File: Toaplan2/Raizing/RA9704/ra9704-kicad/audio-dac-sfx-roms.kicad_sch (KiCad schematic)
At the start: 6 parts, among them U823 YM2151, U827 27C040, U828 M6295, U829 27C040, U830 M6295

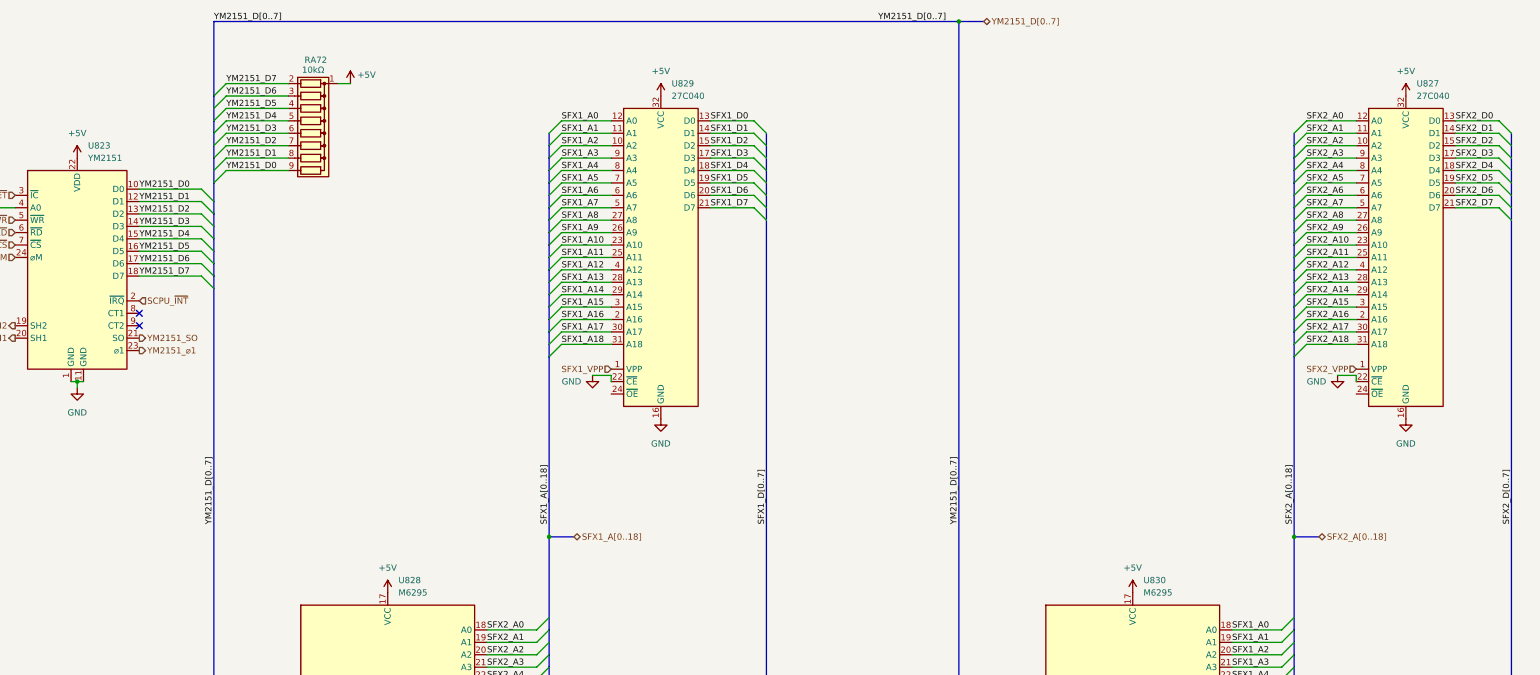
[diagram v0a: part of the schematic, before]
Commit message: fix(ra9704): Add Os as a proxy for 0s in all reference designators
RA9704 has reference designators such that each number has a preceding zero (e.g. RA076, U074, etc.). This causes a bug in KiCAD.

This is 'fixed' by using the 'O' (the letter 'Oh') character instead.

For more info, see the following issue on the KiCAD Gitlab repo

https://gitlab.com/kicad/code/kicad/-/issues/19229
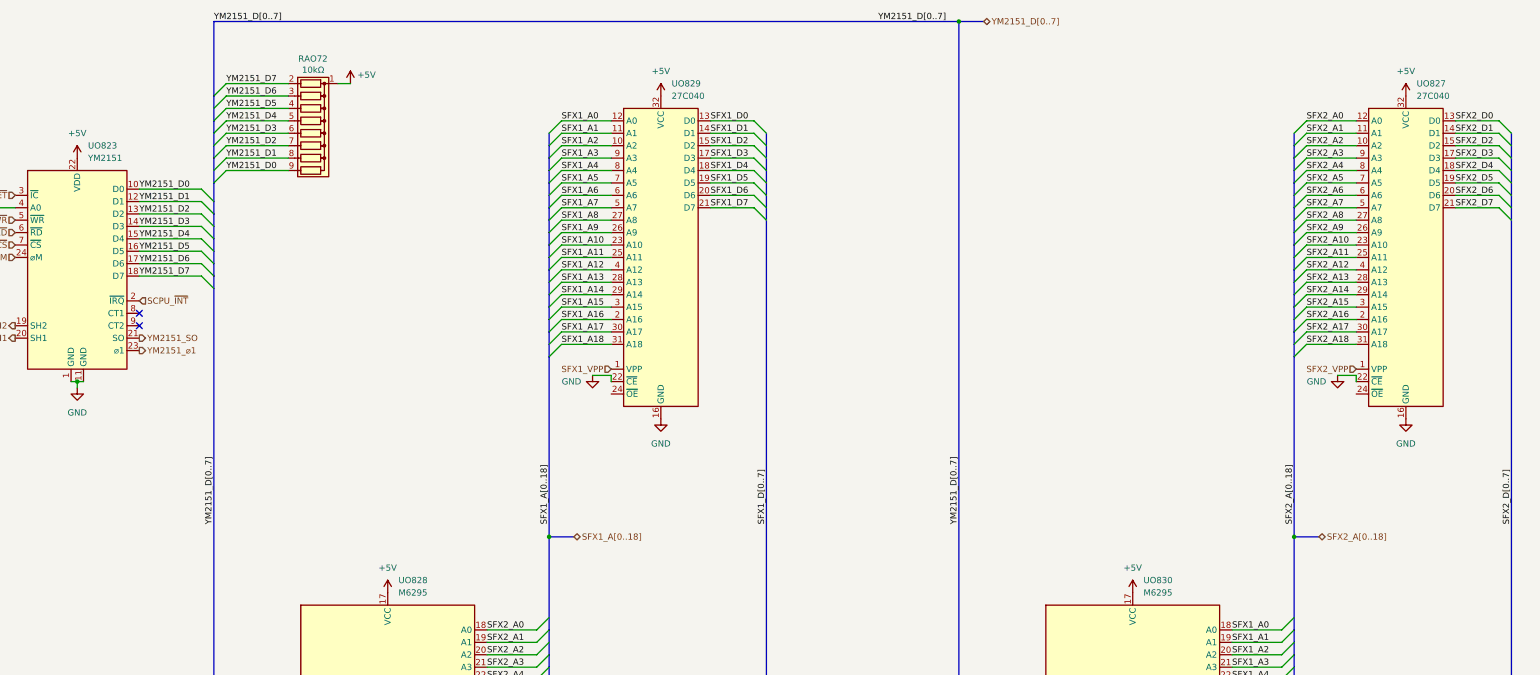
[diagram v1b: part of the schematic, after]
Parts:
- renumbered RA72 to RAO72, U823 to UO823, U827 to UO827, U828 to UO828, U829 to UO829, U830 to UO830
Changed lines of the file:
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@@
 		(dnp no)
 		(fields_autoplaced yes)
-		(property "Reference" "U827"
+		(property "Reference" "UO827"
 			(at 353.9841 35.56 0)
 			(effects
@@
 			(project "ra9704"
 				(path "/24d3b4cf-2360-45fc-8c40-cedc8afdf9e1/748bcde6-3c38-4945-a248-5f19da82ada3"
-					(reference "U827")
+					(reference "UO827")
 					(unit 1)
 				)
@@
 		(on_board yes)
 		(dnp no)
-		(property "Reference" "RA72"
-			(at 126.492 30.734 90)
+		(property "Reference" "RAO72"
+			(at 125.222 30.48 90)
 			(effects
 				(font
@@
 			(project "ra9704"
 				(path "/24d3b4cf-2360-45fc-8c40-cedc8afdf9e1/748bcde6-3c38-4945-a248-5f19da82ada3"
-					(reference "RA72")
+					(reference "RAO72")
 					(unit 1)
 				)
@@
 		(dnp no)
 		(fields_autoplaced yes)
-		(property "Reference" "U829"
+		(property "Reference" "UO829"
 			(at 201.5841 35.56 0)
 			(effects
@@
 			(project "ra9704"
 				(path "/24d3b4cf-2360-45fc-8c40-cedc8afdf9e1/748bcde6-3c38-4945-a248-5f19da82ada3"
-					(reference "U829")
+					(reference "UO829")
 					(unit 1)
 				)
@@
 		(dnp no)
 		(fields_autoplaced yes)
-		(property "Reference" "U830"
+		(property "Reference" "UO830"
 			(at 298.1041 137.16 0)
 			(effects
@@
 			(project "ra9704"
 				(path "/24d3b4cf-2360-45fc-8c40-cedc8afdf9e1/748bcde6-3c38-4945-a248-5f19da82ada3"
-					(reference "U830")
+					(reference "UO830")
 					(unit 1)
 				)
@@
 		(on_board yes)
 		(dnp no)
-		(property "Reference" "U823"
+		(property "Reference" "UO823"
 			(at 82.2041 48.26 0)
 			(effects
@@
 			(project "ra9704"
 				(path "/24d3b4cf-2360-45fc-8c40-cedc8afdf9e1/748bcde6-3c38-4945-a248-5f19da82ada3"
-					(reference "U823")
+					(reference "UO823")
 					(unit 1)
 				)
@@
 		(dnp no)
 		(fields_autoplaced yes)
-		(property "Reference" "U828"
+		(property "Reference" "UO828"
 			(at 145.7041 137.16 0)
 			(effects
@@
 			(project "ra9704"
 				(path "/24d3b4cf-2360-45fc-8c40-cedc8afdf9e1/748bcde6-3c38-4945-a248-5f19da82ada3"
-					(reference "U828")
-					(unit 1)
-				)
+					(reference "UO828")
+					(unit 1)
+				)
